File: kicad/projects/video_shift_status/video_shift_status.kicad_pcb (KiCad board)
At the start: 2 copper layers, 203.2 x 97.8 mm, 25 parts, among them J1 peripheral_addr_bus_connector, J2 peripheral_aux_connector, J3 peripheral_membank_connector, U1 74HC245, U2 74HC245, U3 74HC245, U4 74HC245, U5 74HC245, U6 74HC245, U7 74HC245, U8 74HC245

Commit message: Bit more tweaking and fleshing out of video circuits.
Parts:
- added C10: C, Capacitor_THT:C_Disc_D5.0mm_W2.5mm_P5.00mm, F.Cu at (181.7, 102.4)
- added C11: C, Capacitor_THT:C_Disc_D5.0mm_W2.5mm_P5.00mm, F.Cu at (181.7, 106.4)
- added C12: C, Capacitor_THT:C_Disc_D5.0mm_W2.5mm_P5.00mm, F.Cu at (181.7, 110.5)
- added C13: C, Capacitor_THT:C_Disc_D5.0mm_W2.5mm_P5.00mm, F.Cu at (58.5, 69.8)
- added J4: Conn_01x16_Socket, Connector_PinSocket_2.54mm:PinSocket_1x16_P2.54mm_Horizontal, F.Cu at (160.0, 61.0)
- added J5: Conn_01x16_Socket, Connector_PinSocket_2.54mm:PinSocket_1x16_P2.54mm_Horizontal, F.Cu at (246.4, 61.0)
- added RN1: 10K, Resistor_THT:R_Array_SIP9, F.Cu at (158.8, 78.7)
- added U10: 74HC377, Package_DIP:DIP-20_W7.62mm_Socket, F.Cu at (170.4, 83.0)
- added U11: 74HC138, Package_DIP:DIP-16_W7.62mm_Socket, F.Cu at (68.6, 77.5)
- added U13: 74HC10, Package_DIP:DIP-14_W7.62mm_Socket, F.Cu at (182.2, 83.0)
- added U9: 74HC245, Package_DIP:DIP-20_W7.62mm_Socket, F.Cu at (158.7, 83.0)
- moved C2 6.35 mm to (58.4, 85.1)
- moved C3 6.35 mm to (58.4, 97.8)
- moved C6 6.35 mm to (96.5, 85.1)
- moved C7 6.35 mm to (96.5, 97.8)
- moved U4 6.35 mm to (68.6, 130.8)
- moved U8 6.35 mm to (106.7, 130.8)
- moved C4 6.35 mm to (58.4, 110.5)
- moved C5 6.35 mm to (58.4, 123.2)
- moved C8 6.35 mm to (96.5, 110.5)
- moved C9 6.35 mm to (96.5, 123.2)
- moved U1 6.35 mm to (68.6, 92.7)
- moved U2 6.35 mm to (68.6, 105.4)
- moved U3 6.35 mm to (68.6, 118.1)
- moved U5 6.35 mm to (106.7, 92.7)
- moved U6 6.35 mm to (106.7, 105.4)
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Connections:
- J1 pad 10: /DATA_BUS_09 -> unconnected-(J1-D_09-Pad10)
- J1 pad 11: /DATA_BUS_10 -> unconnected-(J1-D_10-Pad11)
- J1 pad 12: /DATA_BUS_11 -> unconnected-(J1-D_11-Pad12)
- J1 pad 13: /DATA_BUS_12 -> unconnected-(J1-D_12-Pad13)
- J1 pad 14: /DATA_BUS_13 -> unconnected-(J1-D_13-Pad14)
- J1 pad 15: /DATA_BUS_14 -> unconnected-(J1-D_14-Pad15)
- J1 pad 16: /DATA_BUS_15 -> unconnected-(J1-D_15-Pad16)
- J1 pad 17: /ADDR_BUS_00 -> unconnected-(J1-A_00-Pad17)
- J1 pad 18: /ADDR_BUS_01 -> unconnected-(J1-A_01-Pad18)
- J1 pad 19: /ADDR_BUS_02 -> unconnected-(J1-A_02-Pad19)
- J1 pad 20: /ADDR_BUS_03 -> unconnected-(J1-A_03-Pad20)
- J1 pad 21: /ADDR_BUS_04 -> unconnected-(J1-A_04-Pad21)
- J1 pad 22: /ADDR_BUS_05 -> unconnected-(J1-A_05-Pad22)
- J1 pad 23: /ADDR_BUS_06 -> unconnected-(J1-A_06-Pad23)
- J1 pad 24: /ADDR_BUS_07 -> unconnected-(J1-A_07-Pad24)
- J1 pad 25: /ADDR_BUS_08 -> unconnected-(J1-A_08-Pad25)
- J1 pad 26: /ADDR_BUS_09 -> unconnected-(J1-A_09-Pad26)
- J1 pad 27: /ADDR_BUS_10 -> unconnected-(J1-A_10-Pad27)
- J1 pad 28: /ADDR_BUS_11 -> unconnected-(J1-A_11-Pad28)
- J1 pad 29: /ADDR_BUS_12 -> unconnected-(J1-A_12-Pad29)
- J1 pad 30: /ADDR_BUS_13 -> unconnected-(J1-A_13-Pad30)
- J1 pad 31: /ADDR_BUS_14 -> unconnected-(J1-A_14-Pad31)
- J1 pad 32: /ADDR_BUS_15 -> unconnected-(J1-A_15-Pad32)
- J1 pad 6: /DATA_BUS_05 -> unconnected-(J1-D_05-Pad6)
- J1 pad 7: /DATA_BUS_06 -> unconnected-(J1-D_06-Pad7)
- J1 pad 8: /DATA_BUS_07 -> unconnected-(J1-D_07-Pad8)
- J1 pad 9: /DATA_BUS_08 -> unconnected-(J1-D_08-Pad9)
- J2 pad 10: /RFM -> /MEM_ACT
- J2 pad 12: /WTM -> /~{RFM}/WTM
- J2 pad 14: /RESET -> unconnected-(J2-RST-Pad14)
- J2 pad 8: /CTL_CLK -> unconnected-(J2-CCLK-Pad8)
- J3 pad 1: /BANK_BUS_00 -> unconnected-(J3-B_00-Pad1)
- J3 pad 10: /BANK_BUS_09 -> unconnected-(J3-B_09-Pad10)
- J3 pad 11: /BANK_BUS_10 -> unconnected-(J3-B_10-Pad11)
- J3 pad 12: /BANK_BUS_11 -> unconnected-(J3-B_11-Pad12)
- J3 pad 13: /BANK_BUS_12 -> unconnected-(J3-B_12-Pad13)
- J3 pad 14: /BANK_BUS_13 -> unconnected-(J3-B_13-Pad14)
- J3 pad 15: /BANK_BUS_14 -> unconnected-(J3-B_14-Pad15)
- J3 pad 16: /BANK_BUS_15 -> unconnected-(J3-B_15-Pad16)
- J3 pad 2: /BANK_BUS_01 -> unconnected-(J3-B_01-Pad2)
- J3 pad 3: /BANK_BUS_02 -> unconnected-(J3-B_02-Pad3)
- J3 pad 4: /BANK_BUS_03 -> unconnected-(J3-B_03-Pad4)
- J3 pad 5: /BANK_BUS_04 -> unconnected-(J3-B_04-Pad5)
- J3 pad 6: /BANK_BUS_05 -> unconnected-(J3-B_05-Pad6)
- J3 pad 7: /BANK_BUS_06 -> unconnected-(J3-B_06-Pad7)
- J3 pad 8: /BANK_BUS_07 -> unconnected-(J3-B_07-Pad8)
- J3 pad 9: /BANK_BUS_08 -> unconnected-(J3-B_08-Pad9)
- U1 pad 19: unconnected-(U1-~{OE}-Pad19) -> /~{SHIFT_0}
- U2 pad 19: unconnected-(U2-~{OE}-Pad19) -> /~{SHIFT_1}
- U3 pad 19: unconnected-(U3-~{OE}-Pad19) -> /~{SHIFT_2}
- U4 pad 19: unconnected-(U4-~{OE}-Pad19) -> /~{SHIFT_3}
- U5 pad 19: unconnected-(U5-~{OE}-Pad19) -> /~{SHIFT_0}
- U6 pad 19: unconnected-(U6-~{OE}-Pad19) -> /~{SHIFT_1}
- U7 pad 19: unconnected-(U7-~{OE}-Pad19) -> /~{SHIFT_2}
- U8 pad 19: unconnected-(U8-~{OE}-Pad19) -> /~{SHIFT_3}

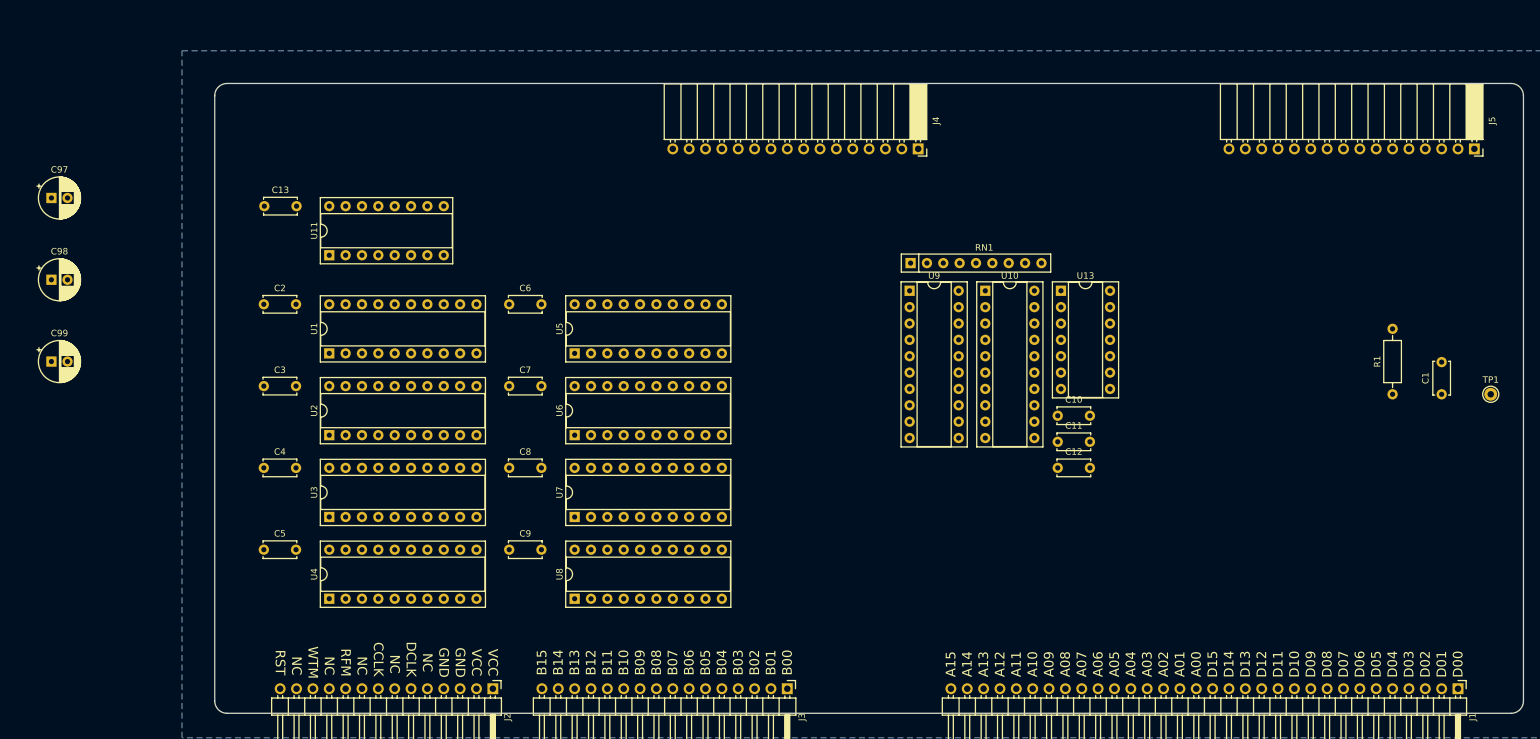
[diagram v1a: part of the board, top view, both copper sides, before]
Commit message: Adding video aux and some bits and bieces on video boards.
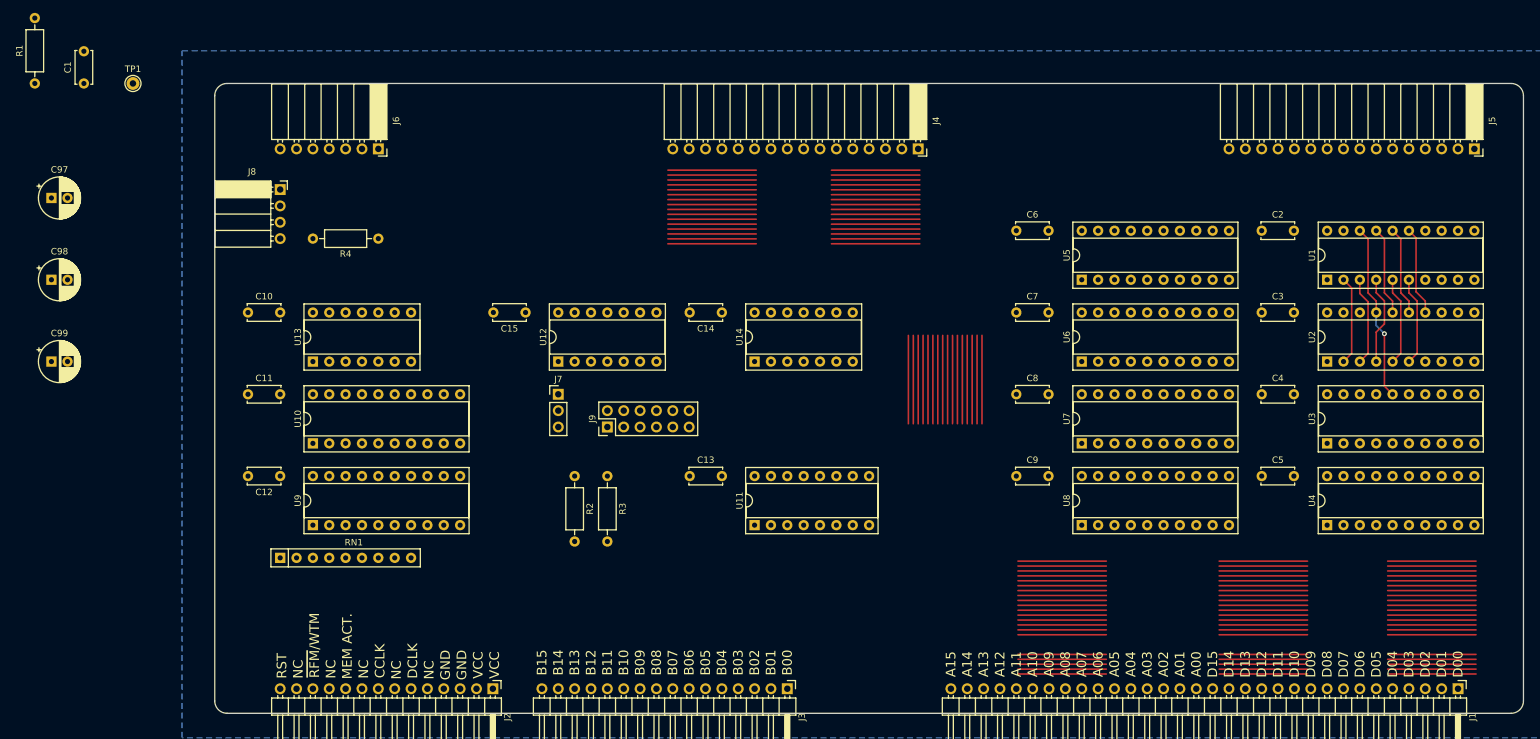
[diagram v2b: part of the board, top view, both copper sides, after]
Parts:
- added C14: C, Capacitor_THT:C_Disc_D5.0mm_W2.5mm_P5.00mm, F.Cu at (129.5, 86.4)
- added C15: C, Capacitor_THT:C_Disc_D5.0mm_W2.5mm_P5.00mm, F.Cu at (99.1, 86.4)
- added J6: video_aux, Connector_PinSocket_2.54mm:PinSocket_1x07_P2.54mm_Horizontal, F.Cu at (76.2, 61.0)
- added J7: Conn_01x03_Pin, Connector_PinHeader_2.54mm:PinHeader_1x03_P2.54mm_Vertical, F.Cu at (104.1, 99.1)
- added J8: Conn_01x04_Socket, Connector_PinSocket_2.54mm:PinSocket_1x04_P2.54mm_Horizontal, F.Cu at (61.0, 67.3)
- added J9: Conn_02x06_Odd_Even, Connector_PinHeader_2.54mm:PinHeader_2x06_P2.54mm_Vertical, F.Cu at (111.8, 104.1)
- added R2: 10K, Resistor_THT:R_Axial_DIN0207_L6.3mm_D2.5mm_P10.16mm_Horizontal, F.Cu at (106.7, 111.8)
- added R3: 10K, Resistor_THT:R_Axial_DIN0207_L6.3mm_D2.5mm_P10.16mm_Horizontal, F.Cu at (111.8, 111.8)
- added R4: 10K, Resistor_THT:R_Axial_DIN0207_L6.3mm_D2.5mm_P10.16mm_Horizontal, F.Cu at (76.2, 74.9)
- added U12: 74HC04, Package_DIP:DIP-14_W7.62mm_Socket, F.Cu at (104.1, 94.0)
- added U14: 74HC04, Package_DIP:DIP-14_W7.62mm_Socket, F.Cu at (134.6, 94.0)
- moved C1 216.3 mm to (30.5, 50.8)
- moved R1 216.3 mm to (22.9, 50.8)
- moved TP1 216.3 mm to (38.1, 50.8)
- moved C2 155.4 mm to (213.4, 73.7)
- moved C3 155.4 mm to (213.4, 86.4)
- moved C4 155.4 mm to (213.4, 99.1)
- moved C5 155.4 mm to (213.4, 111.8)
- moved U1 155.4 mm to (223.5, 81.3)
- moved U2 155.4 mm to (223.5, 94.0)
- moved U3 155.4 mm to (223.5, 106.7)
- moved U4 155.4 mm to (223.5, 119.4)
- moved C10 126.7 mm to (56.0, 86.4)
- moved C11 125.9 mm to (56.0, 99.1)
- moved C12 120.7 mm to (61.0, 111.8), turned to 180 degrees
- moved U13 116.7 mm to (66.0, 94.0), turned to 90 degrees
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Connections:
- J4 pad 1: unconnected-(J4-Pin_1-Pad1) -> /ROW_OUT_0
- J4 pad 10: unconnected-(J4-Pin_10-Pad10) -> /COL_OUT_1
- J4 pad 11: unconnected-(J4-Pin_11-Pad11) -> /COL_OUT_2
- J4 pad 12: unconnected-(J4-Pin_12-Pad12) -> /COL_OUT_3
- J4 pad 13: unconnected-(J4-Pin_13-Pad13) -> /COL_OUT_4
- J4 pad 14: unconnected-(J4-Pin_14-Pad14) -> /COL_OUT_5
- J4 pad 15: unconnected-(J4-Pin_15-Pad15) -> /COL_OUT_6
- J4 pad 16: unconnected-(J4-Pin_16-Pad16) -> /COL_OUT_7
- J4 pad 2: unconnected-(J4-Pin_2-Pad2) -> /ROW_OUT_1
- J4 pad 3: unconnected-(J4-Pin_3-Pad3) -> /ROW_OUT_2
- J4 pad 4: unconnected-(J4-Pin_4-Pad4) -> /ROW_OUT_3
- J4 pad 5: unconnected-(J4-Pin_5-Pad5) -> /ROW_OUT_4
- J4 pad 6: unconnected-(J4-Pin_6-Pad6) -> /ROW_OUT_5
- J4 pad 7: unconnected-(J4-Pin_7-Pad7) -> /ROW_OUT_6
- J4 pad 8: unconnected-(J4-Pin_8-Pad8) -> /ROW_OUT_7
- J4 pad 9: unconnected-(J4-Pin_9-Pad9) -> /COL_OUT_0
- J5 pad 1: unconnected-(J5-Pin_1-Pad1) -> /ROW_IN_0
- J5 pad 10: unconnected-(J5-Pin_10-Pad10) -> /COL_IN_1
- J5 pad 11: unconnected-(J5-Pin_11-Pad11) -> /COL_IN_2
- J5 pad 12: unconnected-(J5-Pin_12-Pad12) -> /COL_IN_3
- J5 pad 13: unconnected-(J5-Pin_13-Pad13) -> /COL_IN_4
- J5 pad 14: unconnected-(J5-Pin_14-Pad14) -> /COL_IN_5
- J5 pad 15: unconnected-(J5-Pin_15-Pad15) -> /COL_IN_6
- J5 pad 16: unconnected-(J5-Pin_16-Pad16) -> /COL_IN_7
- J5 pad 2: unconnected-(J5-Pin_2-Pad2) -> /ROW_IN_1
- J5 pad 3: unconnected-(J5-Pin_3-Pad3) -> /ROW_IN_2
- J5 pad 4: unconnected-(J5-Pin_4-Pad4) -> /ROW_IN_3
- J5 pad 5: unconnected-(J5-Pin_5-Pad5) -> /ROW_IN_4
- J5 pad 6: unconnected-(J5-Pin_6-Pad6) -> /ROW_IN_5
- J5 pad 7: unconnected-(J5-Pin_7-Pad7) -> /ROW_IN_6
- J5 pad 8: unconnected-(J5-Pin_8-Pad8) -> /ROW_IN_7
- J5 pad 9: unconnected-(J5-Pin_9-Pad9) -> /COL_IN_0
- U1 pad 11: /ROW_IN_00 -> /ROW_IN_0
- U1 pad 12: /ROW_IN_01 -> /ROW_IN_1
- U1 pad 13: /ROW_IN_02 -> /ROW_IN_2
- U1 pad 14: /ROW_IN_03 -> /ROW_IN_3
- U1 pad 15: /ROW_IN_04 -> /ROW_IN_4
- U1 pad 16: /ROW_IN_05 -> /ROW_IN_5
- U1 pad 17: /ROW_IN_06 -> /ROW_IN_6
- U1 pad 18: /ROW_IN_07 -> /ROW_IN_7
- U1 pad 2: /ROW_OUT_07 -> /ROW_OUT_7
- U1 pad 3: /ROW_OUT_06 -> /ROW_OUT_6
- U1 pad 4: /ROW_OUT_05 -> /ROW_OUT_5
- U1 pad 5: /ROW_OUT_04 -> /ROW_OUT_4
- U1 pad 6: /ROW_OUT_03 -> /ROW_OUT_3
- U1 pad 7: /ROW_OUT_02 -> /ROW_OUT_2
- U1 pad 8: /ROW_OUT_01 -> /ROW_OUT_1
- U1 pad 9: /ROW_OUT_00 -> /ROW_OUT_0
- U10 pad 14: /DATA_BUS_02 -> GND
- U10 pad 15: /BANK_SEL -> unconnected-(U10-Q5-Pad15)
- U10 pad 16: /SHIFT_SEL_1 -> unconnected-(U10-Q6-Pad16)
- U10 pad 17: /DATA_BUS_01 -> GND
- U10 pad 18: /DATA_BUS_00 -> GND
- U10 pad 19: /SHIFT_SEL_0 -> unconnected-(U10-Q7-Pad19)
- U10 pad 2: unconnected-(U10-Q0-Pad2) -> /BANK_SEL
- U10 pad 3: GND -> /DATA_BUS_02
- U10 pad 4: GND -> /DATA_BUS_01
- U10 pad 5: unconnected-(U10-Q1-Pad5) -> /SHIFT_SEL_1
- U10 pad 6: unconnected-(U10-Q2-Pad6) -> /SHIFT_SEL_0
- U10 pad 7: GND -> /DATA_BUS_00
- U2 pad 11: /ROW_IN_01 -> /ROW_IN_1
- U2 pad 12: /ROW_IN_02 -> /ROW_IN_2
- U2 pad 13: /ROW_IN_03 -> /ROW_IN_3
- U2 pad 14: /ROW_IN_04 -> /ROW_IN_4
- U2 pad 15: /ROW_IN_05 -> /ROW_IN_5
- U2 pad 16: /ROW_IN_06 -> /ROW_IN_6
- U2 pad 17: /ROW_IN_07 -> /ROW_IN_7
- U2 pad 2: /ROW_OUT_07 -> /ROW_OUT_7
- U2 pad 3: /ROW_OUT_06 -> /ROW_OUT_6
- U2 pad 4: /ROW_OUT_05 -> /ROW_OUT_5
- U2 pad 5: /ROW_OUT_04 -> /ROW_OUT_4
- U2 pad 6: /ROW_OUT_03 -> /ROW_OUT_3
- U2 pad 7: /ROW_OUT_02 -> /ROW_OUT_2
- U2 pad 8: /ROW_OUT_01 -> /ROW_OUT_1
- U2 pad 9: /ROW_OUT_00 -> /ROW_OUT_0
- U3 pad 11: /ROW_IN_02 -> /ROW_IN_2
- U3 pad 12: /ROW_IN_03 -> /ROW_IN_3
- U3 pad 13: /ROW_IN_04 -> /ROW_IN_4
- U3 pad 14: /ROW_IN_05 -> /ROW_IN_5
- U3 pad 15: /ROW_IN_06 -> /ROW_IN_6
- U3 pad 16: /ROW_IN_07 -> /ROW_IN_7
- U3 pad 2: /ROW_OUT_07 -> /ROW_OUT_7
- U3 pad 3: /ROW_OUT_06 -> /ROW_OUT_6
- U3 pad 4: /ROW_OUT_05 -> /ROW_OUT_5
- U3 pad 5: /ROW_OUT_04 -> /ROW_OUT_4
- U3 pad 6: /ROW_OUT_03 -> /ROW_OUT_3
- U3 pad 7: /ROW_OUT_02 -> /ROW_OUT_2
- U3 pad 8: /ROW_OUT_01 -> /ROW_OUT_1
- U3 pad 9: /ROW_OUT_00 -> /ROW_OUT_0
- U4 pad 11: /ROW_IN_03 -> /ROW_IN_3
- U4 pad 12: /ROW_IN_04 -> /ROW_IN_4
- U4 pad 13: /ROW_IN_05 -> /ROW_IN_5
- U4 pad 14: /ROW_IN_06 -> /ROW_IN_6
- U4 pad 15: /ROW_IN_07 -> /ROW_IN_7
- U4 pad 2: /ROW_OUT_07 -> /ROW_OUT_7
- U4 pad 3: /ROW_OUT_06 -> /ROW_OUT_6
- U4 pad 4: /ROW_OUT_05 -> /ROW_OUT_5
- U4 pad 5: /ROW_OUT_04 -> /ROW_OUT_4
- U4 pad 6: /ROW_OUT_03 -> /ROW_OUT_3
- U4 pad 7: /ROW_OUT_02 -> /ROW_OUT_2
- U4 pad 8: /ROW_OUT_01 -> /ROW_OUT_1
- U4 pad 9: /ROW_OUT_00 -> /ROW_OUT_0
- U5 pad 11: /COL_IN_00 -> /COL_IN_0
- U5 pad 12: /COL_IN_01 -> /COL_IN_1
- U5 pad 13: /COL_IN_02 -> /COL_IN_2
- U5 pad 14: /COL_IN_03 -> /COL_IN_3
- U5 pad 15: /COL_IN_04 -> /COL_IN_4
- U5 pad 16: /COL_IN_05 -> /COL_IN_5
- U5 pad 17: /COL_IN_06 -> /COL_IN_6
- U5 pad 18: /COL_IN_07 -> /COL_IN_7
- U5 pad 2: /COL_OUT_07 -> /COL_OUT_7
- U5 pad 3: /COL_OUT_06 -> /COL_OUT_6
- U5 pad 4: /COL_OUT_05 -> /COL_OUT_5
- U5 pad 5: /COL_OUT_04 -> /COL_OUT_4
- U5 pad 6: /COL_OUT_03 -> /COL_OUT_3
- U5 pad 7: /COL_OUT_02 -> /COL_OUT_2
- U5 pad 8: /COL_OUT_01 -> /COL_OUT_1
- U5 pad 9: /COL_OUT_00 -> /COL_OUT_0
- U6 pad 11: /COL_IN_01 -> /COL_IN_1
- U6 pad 12: /COL_IN_02 -> /COL_IN_2
- U6 pad 13: /COL_IN_03 -> /COL_IN_3
- U6 pad 14: /COL_IN_04 -> /COL_IN_4
- U6 pad 15: /COL_IN_05 -> /COL_IN_5
- U6 pad 16: /COL_IN_06 -> /COL_IN_6
- U6 pad 17: /COL_IN_07 -> /COL_IN_7
- U6 pad 2: /COL_OUT_07 -> /COL_OUT_7
- U6 pad 3: /COL_OUT_06 -> /COL_OUT_6
- U6 pad 4: /COL_OUT_05 -> /COL_OUT_5
- U6 pad 5: /COL_OUT_04 -> /COL_OUT_4
- U6 pad 6: /COL_OUT_03 -> /COL_OUT_3
- U6 pad 7: /COL_OUT_02 -> /COL_OUT_2
- U6 pad 8: /COL_OUT_01 -> /COL_OUT_1
- U6 pad 9: /COL_OUT_00 -> /COL_OUT_0
- U7 pad 11: /COL_IN_02 -> /COL_IN_2
- U7 pad 12: /COL_IN_03 -> /COL_IN_3
- U7 pad 13: /COL_IN_04 -> /COL_IN_4
- U7 pad 14: /COL_IN_05 -> /COL_IN_5
- U7 pad 15: /COL_IN_06 -> /COL_IN_6
- U7 pad 16: /COL_IN_07 -> /COL_IN_7
- U7 pad 2: /COL_OUT_07 -> /COL_OUT_7
- U7 pad 3: /COL_OUT_06 -> /COL_OUT_6
- U7 pad 4: /COL_OUT_05 -> /COL_OUT_5
- U7 pad 5: /COL_OUT_04 -> /COL_OUT_4
- U7 pad 6: /COL_OUT_03 -> /COL_OUT_3
- U7 pad 7: /COL_OUT_02 -> /COL_OUT_2
- U7 pad 8: /COL_OUT_01 -> /COL_OUT_1
- U7 pad 9: /COL_OUT_00 -> /COL_OUT_0
- U8 pad 11: /COL_IN_03 -> /COL_IN_3
- U8 pad 12: /COL_IN_04 -> /COL_IN_4
- U8 pad 13: /COL_IN_05 -> /COL_IN_5
- U8 pad 14: /COL_IN_06 -> /COL_IN_6
- U8 pad 15: /COL_IN_07 -> /COL_IN_7
- U8 pad 2: /COL_OUT_07 -> /COL_OUT_7
- U8 pad 3: /COL_OUT_06 -> /COL_OUT_6
- U8 pad 4: /COL_OUT_05 -> /COL_OUT_5
- U8 pad 5: /COL_OUT_04 -> /COL_OUT_4
- U8 pad 6: /COL_OUT_03 -> /COL_OUT_3
- U8 pad 7: /COL_OUT_02 -> /COL_OUT_2
- U8 pad 8: /COL_OUT_01 -> /COL_OUT_1
- U8 pad 9: /COL_OUT_00 -> /COL_OUT_0
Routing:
- net /ROW_OUT_7: track 0.00 -> 96.0 mm
- net /ROW_OUT_6: track 0.00 -> 96.0 mm
- net /ROW_OUT_5: track 0.00 -> 96.0 mm
- net /ROW_OUT_3: track 0.00 -> 96.0 mm
- net /ROW_OUT_4: track 0.00 -> 96.0 mm
- net /ROW_OUT_2: track 0.00 -> 82.3 mm
- net /ROW_OUT_1: track 0.00 -> 82.3 mm
- net /ROW_OUT_0: track 0.00 -> 82.3 mm
- net /COL_OUT_7: track 0.00 -> 82.3 mm
- net /COL_OUT_6: track 0.00 -> 82.3 mm
- net /COL_OUT_5: track 0.00 -> 82.3 mm
- net /COL_OUT_4: track 0.00 -> 82.3 mm
- net /COL_OUT_3: track 0.00 -> 82.3 mm
- net /COL_OUT_2: track 0.00 -> 82.3 mm
- net /COL_OUT_1: track 0.00 -> 82.3 mm
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
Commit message: Start PCB for video timing.
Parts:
- moved J4 15.2 mm to (144.8, 61.0)
- moved C8 7.13 mm to (180.3, 104.1), turned to 90 degrees
- moved C9 7.13 mm to (180.3, 116.8), turned to 90 degrees
- moved C10 7.07 mm to (61.0, 91.4), turned to 90 degrees
- moved C11 7.07 mm to (61.0, 104.1), turned to 90 degrees
- moved C4 7.07 mm to (218.4, 104.1), turned to 90 degrees
- moved C5 7.07 mm to (218.4, 116.8), turned to 90 degrees
- moved C6 7.07 mm to (180.3, 78.7), turned to 90 degrees
- moved C7 7.07 mm to (180.3, 91.4), turned to 90 degrees
- moved C13 7.07 mm to (129.5, 116.8), turned to 90 degrees
- moved C2 5.08 mm to (218.4, 73.7), turned to -90 degrees
- moved C3 5.08 mm to (218.4, 86.4), turned to -90 degrees
- moved J6 2.54 mm to (73.7, 61.0)
- turned C12 to -90 degrees
- turned C14 to -90 degrees
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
